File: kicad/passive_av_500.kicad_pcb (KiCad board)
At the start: 2 copper layers, 57.1 x 29.8 mm, 22 parts, among them J1 Raspberry_Pi_5, J2 Conn_Coaxial, J3 Conn_01x05, J4 AudioJack4

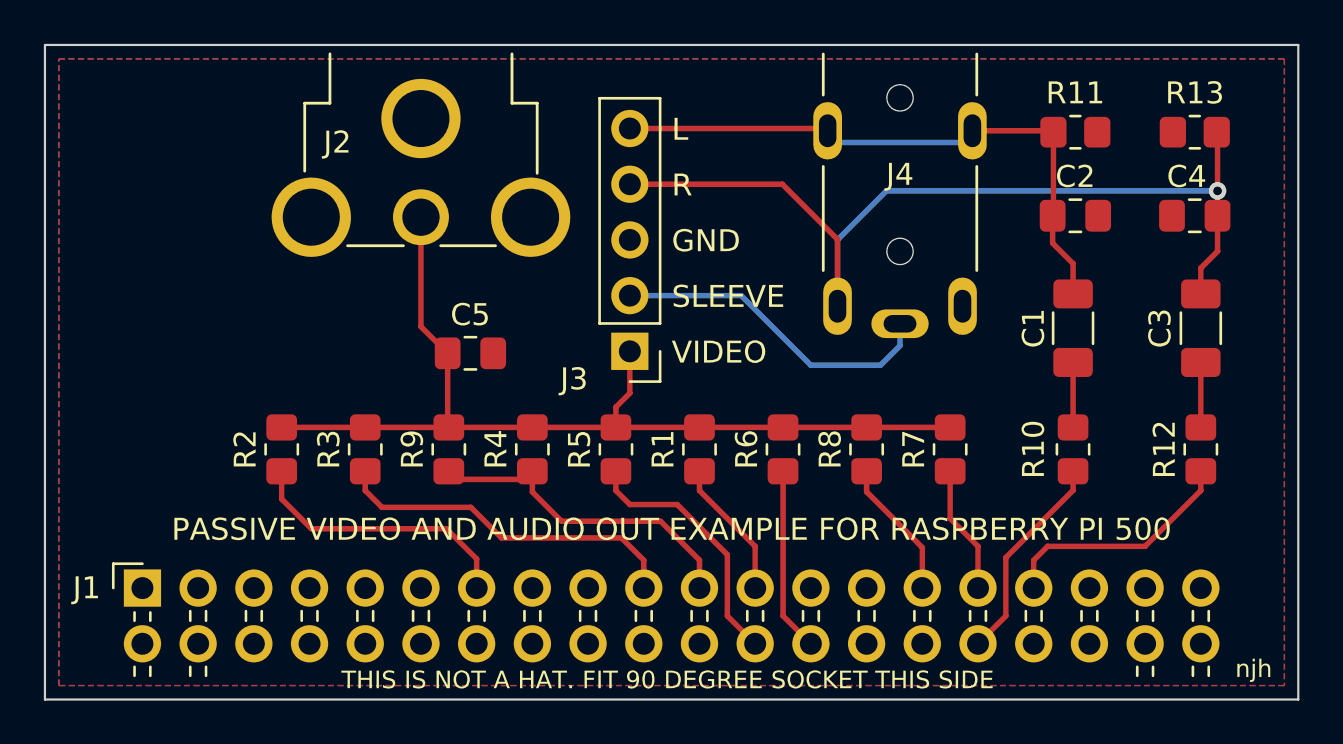
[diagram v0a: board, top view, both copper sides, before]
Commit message: Add "tooling holes" and reconnect J1 pin 39 to improve GND plane
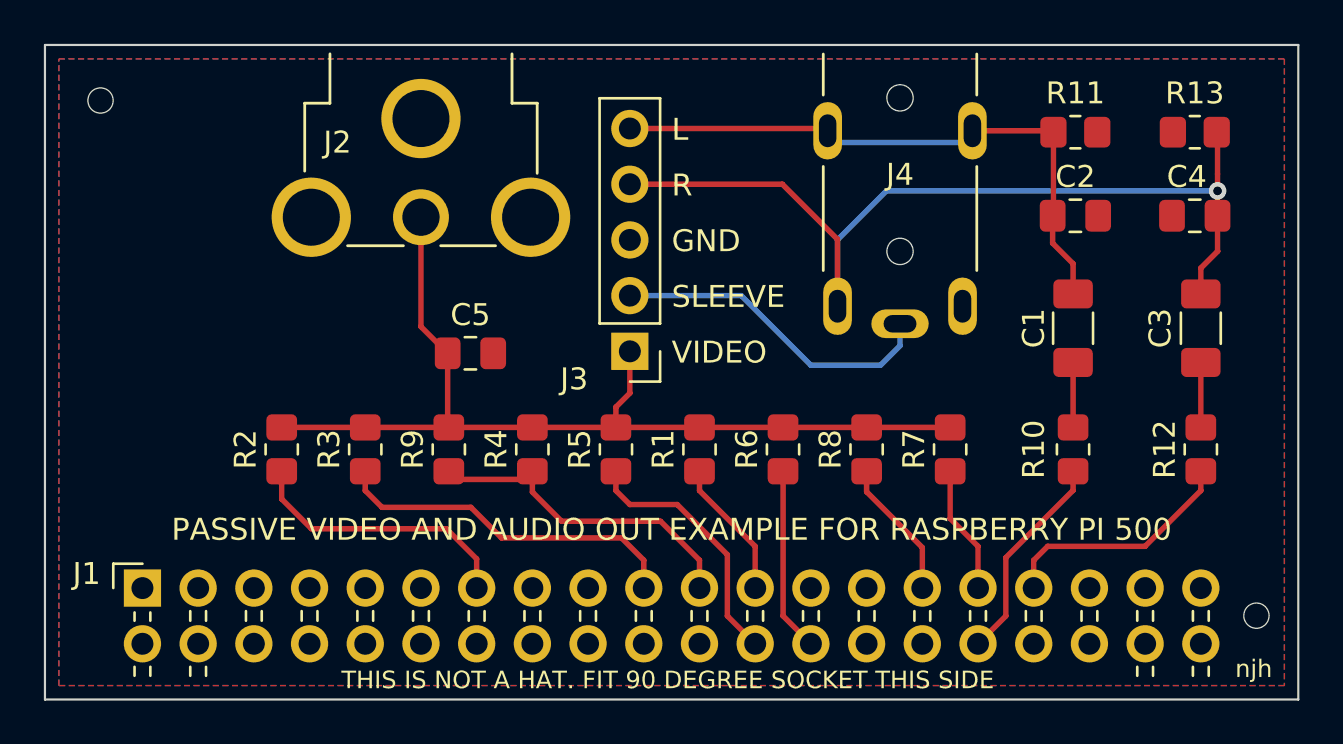
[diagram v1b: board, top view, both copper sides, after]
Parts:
- added H1: MountingHole, MountingHole:ToolingHole_1.152mm, F.Cu at (40.6, 30.5)
- added H2: MountingHole, MountingHole:ToolingHole_1.152mm, F.Cu at (93.3, 54.0)
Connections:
- J1 pad 39: unconnected-(J1-GND-Pad39) -> GND
